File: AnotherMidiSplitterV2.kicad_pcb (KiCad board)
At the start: 2 copper layers, 65 x 98 mm, 44 parts, among them J1 IN, J10 OUT, J11 OUT, J2 USB_power, J4 OUT, J5 OUT, J6 OUT, J7 OUT, J8 OUT, J9 OUT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

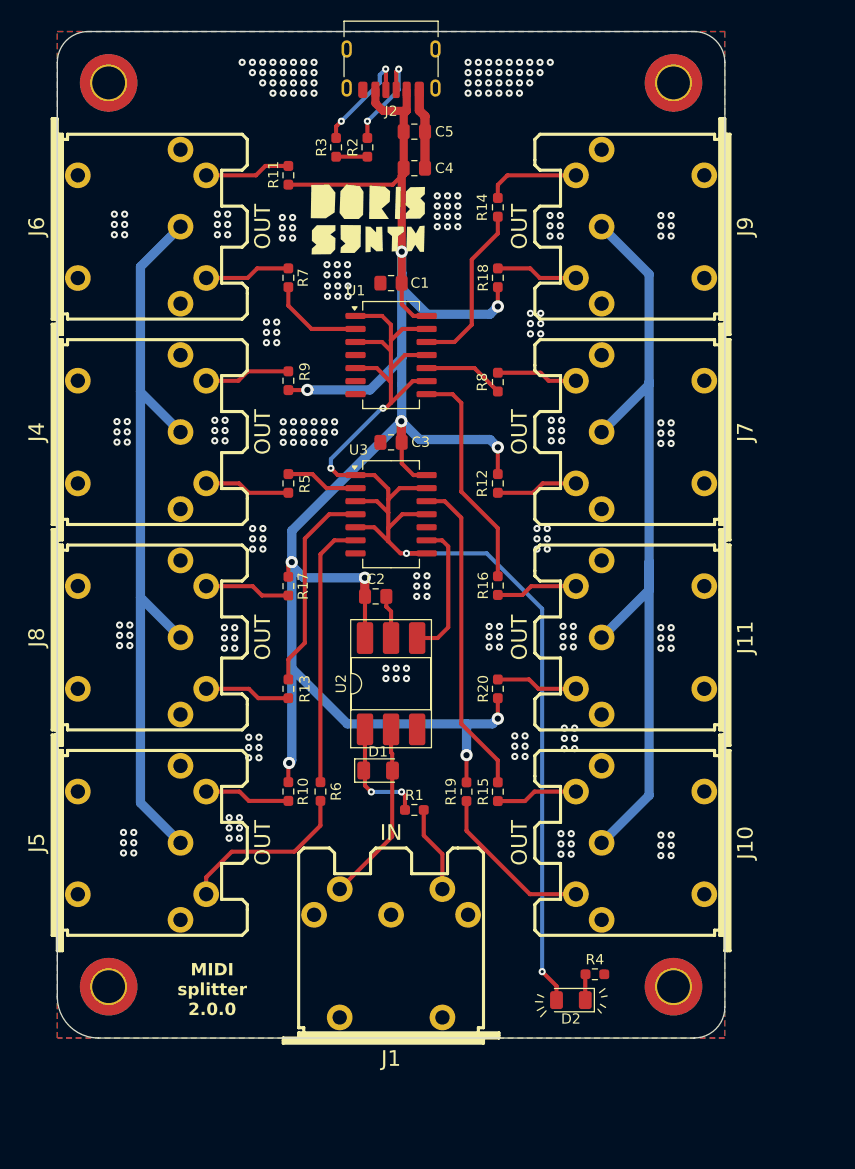
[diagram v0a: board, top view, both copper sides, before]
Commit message: change elements to tht update layout
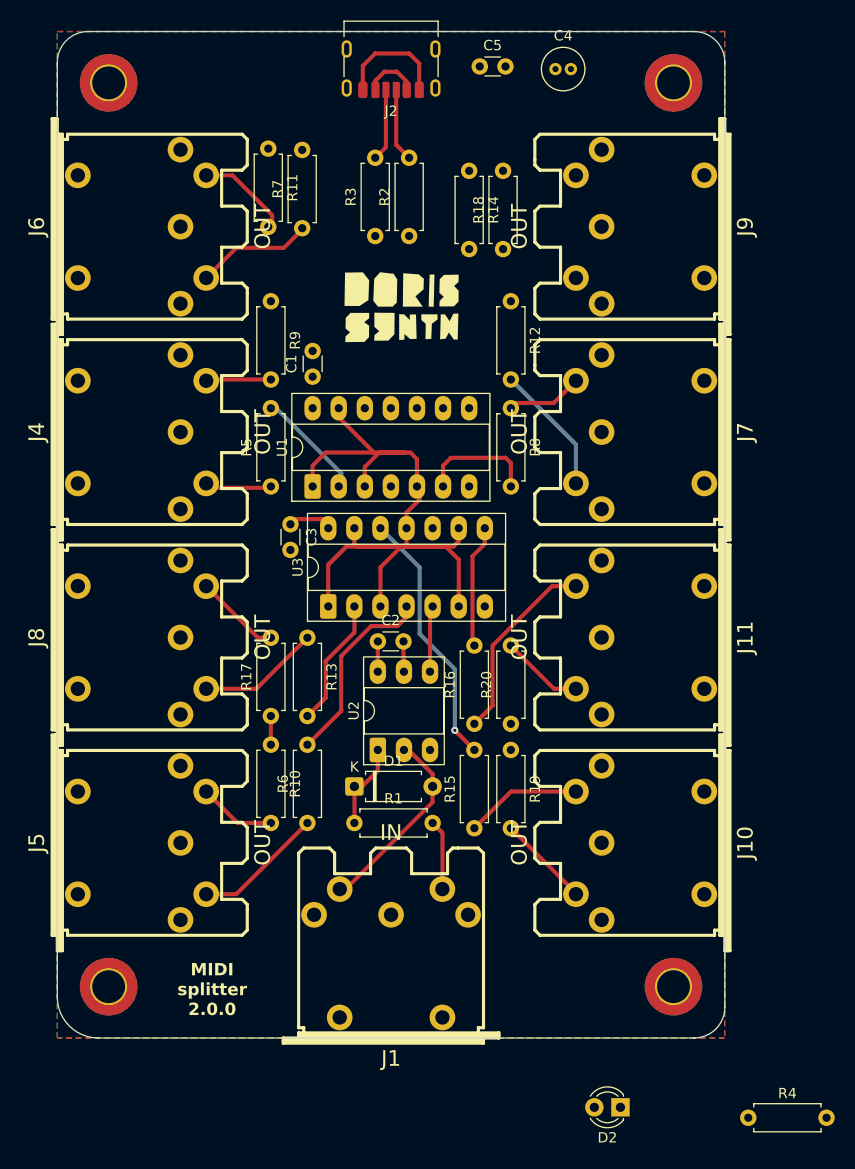
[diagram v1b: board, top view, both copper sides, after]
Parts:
- C1, C2, C3, C5: footprint Capacitor_SMD:C_0805_2012Metric_Pad1.18x1.45mm_HandSolder -> Capacitor_THT:C_Disc_D3.0mm_W1.6mm_P2.50mm
- C4: footprint Capacitor_SMD:C_0805_2012Metric_Pad1.18x1.45mm_HandSolder -> Capacitor_THT:C_Radial_D4.0mm_H5.0mm_P1.50mm
- D1: footprint Diode_SMD:D_1206_3216Metric -> Diode_THT:D_A-405_P7.62mm_Horizontal
- D2: footprint LED_SMD:LED_1206_3216Metric -> LED_THT:LED_D3.0mm
- R1, R10, R11, R12, R13, R14, R15, R16, R17, R18, R19, R2, R20, R3, R4, R5, R6, R7, R8, R9: footprint Resistor_SMD:R_0603_1608Metric_Pad0.98x0.95mm_HandSolder -> Resistor_THT:R_Axial_DIN0207_L6.3mm_D2.5mm_P7.62mm_Horizontal
- U1, U3: footprint Package_SO:SO-14_5.3x10.2mm_P1.27mm -> Package_DIP:CERDIP-14_W7.62mm_SideBrazed_LongPads_Socket
- U2: footprint Package_DIP:DIP-6_W8.89mm_SMDSocket_LongPads -> Package_DIP:DIP-6_W7.62mm_Socket_LongPads
- moved R4 20.5 mm to (208.3, 143.8)
- moved R12 17.8 mm to (185.2, 64.3)
- moved C4 16.8 mm to (189.5, 41.7)
- moved U1 14.9 mm to (165.9, 82.3), turned to 90 degrees
- moved R16 13.7 mm to (181.6, 105.4)
- moved R17 12.8 mm to (161.8, 104.6), turned to 90 degrees
- moved C3 12.6 mm to (163.7, 86.0), turned to -90 degrees
- moved C1 11.9 mm to (165.9, 71.6), turned to 90 degrees
- moved D2 11.5 mm to (195.8, 142.7)
- moved U3 10.9 mm to (167.4, 94.0), turned to 90 degrees
- moved R2 9.54 mm to (175.3, 57.9)
- moved R3 9.44 mm to (172.0, 57.9)
- moved C5 8.99 mm to (182.1, 41.4)
- moved R9 7.92 mm to (161.8, 64.3), turned to -90 degrees
- moved U2 6.58 mm to (172.2, 108.0)
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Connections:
- R14 pad 2: Net-(R14-Pad2) -> unconnected-(R14-Pad2)
- U1 pad 10: Net-(R8-Pad2) -> unconnected-(U1-Pad10)
- U1 pad 11: /MIDI_SIG -> unconnected-(U1-Pad11)
- U1 pad 12: Net-(R14-Pad2) -> Net-(R7-Pad2)
- U1 pad 2: Net-(R7-Pad2) -> Net-(R5-Pad2)
- U1 pad 6: unconnected-(U1-Pad6) -> Net-(R8-Pad2)
- U1 pad 8: Net-(R16-Pad2) -> unconnected-(U1-Pad8)
- U1 pad 9: /MIDI_SIG -> unconnected-(U1-Pad9)
- U3 pad 2: Net-(R5-Pad2) -> Net-(R13-Pad2)
- U3 pad 4: Net-(R13-Pad2) -> Net-(R6-Pad2)
- U3 pad 5: /MIDI_SIG -> Net-(U2-Pad4)
- U3 pad 6: Net-(R6-Pad2) -> /MIDI_SIG
- U3 pad 8: /MIDI_SIG -> Net-(R16-Pad2)
- U3 pad 9: Net-(U2-Pad4) -> /MIDI_SIG
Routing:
- net +5V: track 188.2 -> 15.7 mm, vias 10 -> 0
- net GND: track 169.3 -> 14.3 mm, vias 259 -> 0
- net /MIDI_SIG: track 128.3 -> 77.3 mm, vias 4 -> 0
- net Net-(R14-Pad2): track 16.7 -> 0.00 mm
- net Net-(J11-Pad4): track 7.96 -> 18.9 mm
- net Net-(R16-Pad2): track 22.1 -> 12.0 mm
- net Net-(R7-Pad2): track 9.28 -> 0.00 mm
- net Net-(J9-Pad4): track 9.26 -> 0.00 mm
- net Net-(J9-Pad5): track 7.99 -> 0.00 mm
- net Net-(R13-Pad2): track 20.3 -> 12.6 mm
- net Net-(U2-Pad4): track 13.7 -> 6.46 mm
- net Net-(R6-Pad2): track 26.2 -> 18.9 mm
- net Net-(J10-Pad5): track 16.1 -> 9.05 mm
- net Net-(R15-Pad2): track 31.3 -> 25.4 mm, vias 0 -> 1
- net Net-(J7-Pad5): track 7.98 -> 12.7 mm
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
